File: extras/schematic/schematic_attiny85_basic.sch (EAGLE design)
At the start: 21 parts, among them SW1 Seek Down, SW2 Seek Up, U1 SI4735-D60-GU, U2 ATTINY85-P

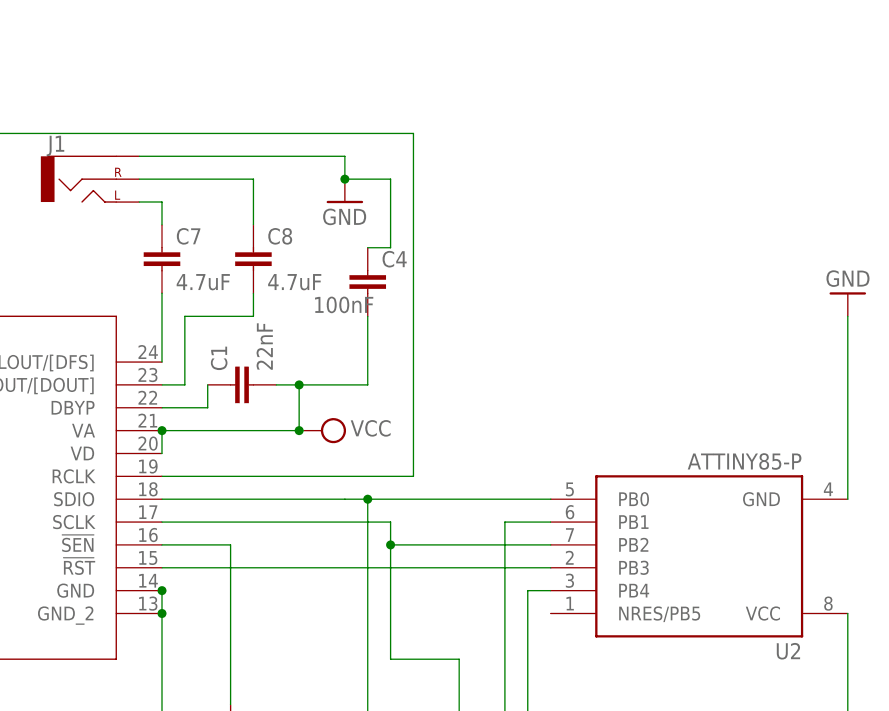
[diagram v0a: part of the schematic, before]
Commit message: SI473X Arduino Library
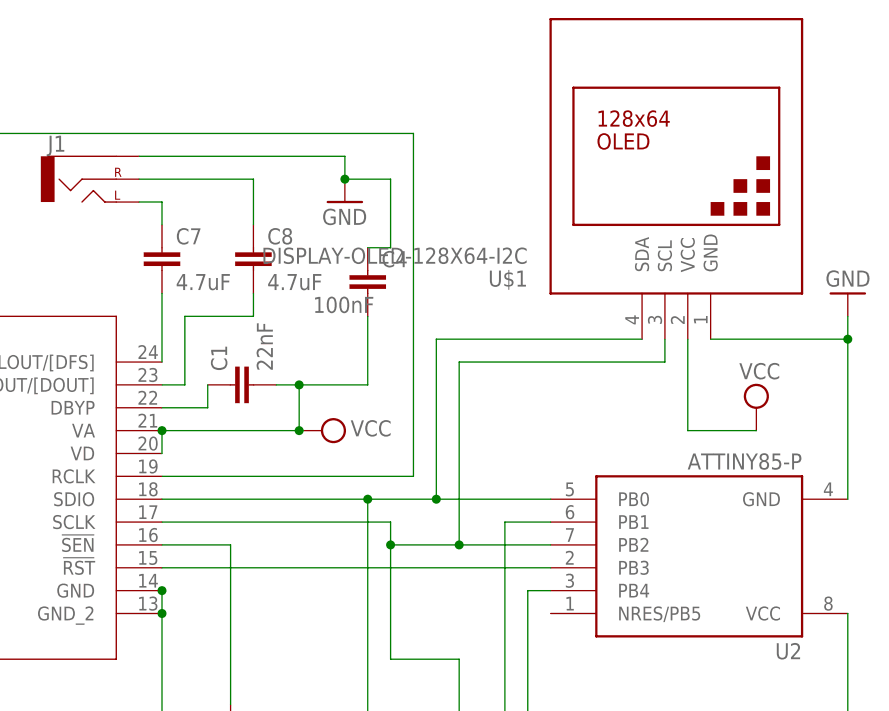
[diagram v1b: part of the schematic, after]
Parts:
- added U$1: DISPLAY-OLED-128X64-I2C, diy-modules:DISPLAY-OLED-128X64-I2C
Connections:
- net GND: now also U$1.GND
- net N$15: now also U$1.SDA
- net SDA: now also U$1.SCL
- net VCC: now also U$1.VCC
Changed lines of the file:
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@@
 <part name="SW2" library="adafruit" library_urn="urn:adsk.eagle:library:420" deviceset="SWITCH_PUSHBUTTON" device="EVQ-PE" package3d_urn="urn:adsk.eagle:package:6240957/1" value="Seek Up"/>
 <part name="GND6" library="supply1" library_urn="urn:adsk.eagle:library:371" deviceset="GND" device=""/>
+<part name="U$1" library="diy-modules" deviceset="DISPLAY-OLED-128X64-I2C" device=""/>
+<part name="SUPPLY2" library="supply2" library_urn="urn:adsk.eagle:library:372" deviceset="VCC" device=""/>
 </parts>
 <sheets>
@@
 <attribute name="VALUE" x="83.82" y="63.5" size="1.778" layer="96"/>
 </instance>
+<instance part="U$1" gate="G$1" x="88.9" y="139.7" smashed="yes" rot="R180">
+<attribute name="NAME" x="73.66" y="127" size="1.778" layer="95" rot="R180"/>
+<attribute name="VALUE" x="73.66" y="129.54" size="1.778" layer="96" rot="R180"/>
+</instance>
+<instance part="SUPPLY2" gate="G$1" x="99.06" y="111.76" smashed="yes">
+<attribute name="VALUE" x="97.155" y="114.935" size="1.778" layer="96"/>
+</instance>
 </instances>
 <busses>
@@
 <pinref part="U2" gate="G$1" pin="GND"/>
 <pinref part="GND2" gate="1" pin="GND"/>
-<wire x1="109.22" y1="101.6" x2="109.22" y2="121.92" width="0.1524" layer="91"/>
+<wire x1="109.22" y1="101.6" x2="109.22" y2="119.38" width="0.1524" layer="91"/>
+<pinref part="U$1" gate="G$1" pin="GND"/>
+<wire x1="109.22" y1="119.38" x2="109.22" y2="121.92" width="0.1524" layer="91"/>
+<wire x1="93.98" y1="119.38" x2="109.22" y2="119.38" width="0.1524" layer="91"/>
+<junction x="109.22" y="119.38"/>
 </segment>
 <segment>
@@
 <wire x1="58.42" y1="99.06" x2="33.02" y2="99.06" width="0.1524" layer="91"/>
 <pinref part="U2" gate="G$1" pin="PB2"/>
-<wire x1="76.2" y1="96.52" x2="58.42" y2="96.52" width="0.1524" layer="91"/>
+<wire x1="76.2" y1="96.52" x2="66.04" y2="96.52" width="0.1524" layer="91"/>
 <junction x="58.42" y="96.52"/>
+<pinref part="U$1" gate="G$1" pin="SCL"/>
+<wire x1="66.04" y1="96.52" x2="58.42" y2="96.52" width="0.1524" layer="91"/>
+<wire x1="88.9" y1="119.38" x2="88.9" y2="116.84" width="0.1524" layer="91"/>
+<wire x1="88.9" y1="116.84" x2="66.04" y2="116.84" width="0.1524" layer="91"/>
+<wire x1="66.04" y1="116.84" x2="66.04" y2="96.52" width="0.1524" layer="91"/>
+<junction x="66.04" y="96.52"/>
 </segment>
 </net>
@@
 <pinref part="SUPPLY4" gate="G$1" pin="VCC"/>
 </segment>
+<segment>
+<pinref part="U$1" gate="G$1" pin="VCC"/>
+<wire x1="91.44" y1="119.38" x2="91.44" y2="109.22" width="0.1524" layer="91"/>
+<pinref part="SUPPLY2" gate="G$1" pin="VCC"/>
+<wire x1="91.44" y1="109.22" x2="99.06" y2="109.22" width="0.1524" layer="91"/>
+</segment>
 </net>
 <net name="N$4" class="0">
@@
 <pinref part="R4" gate="G$1" pin="2"/>
 <pinref part="U1" gate="A" pin="SDIO"/>
-<wire x1="33.02" y1="101.6" x2="53.34" y2="101.6" width="0.1524" layer="91"/>
-<wire x1="53.34" y1="101.6" x2="55.88" y2="101.6" width="0.1524" layer="91"/>
+<wire x1="33.02" y1="101.6" x2="55.88" y2="101.6" width="0.1524" layer="91"/>
 <wire x1="55.88" y1="101.6" x2="55.88" y2="73.66" width="0.1524" layer="91"/>
 <pinref part="U2" gate="G$1" pin="PB0"/>
-<wire x1="76.2" y1="101.6" x2="55.88" y2="101.6" width="0.1524" layer="91"/>
+<wire x1="76.2" y1="101.6" x2="63.5" y2="101.6" width="0.1524" layer="91"/>
 <junction x="55.88" y="101.6"/>
-</segment>
-</net>
+<pinref part="U$1" gate="G$1" pin="SDA"/>
+<wire x1="63.5" y1="101.6" x2="55.88" y2="101.6" width="0.1524" layer="91"/>
+<wire x1="86.36" y1="119.38" x2="63.5" y2="119.38" width="0.1524" layer="91"/>
+<wire x1="63.5" y1="119.38" x2="63.5" y2="101.6" width="0.1524" layer="91"/>
+<junction x="63.5" y="101.6"/>
+</segment>
+</net>
